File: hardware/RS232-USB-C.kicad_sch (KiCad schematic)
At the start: 68 parts, among them J1 USB_C_Receptacle_USB2.0_16P, J10 NC, J11 UART, J12 NC, J13 NC, J2 DE9_Receptacle, J3 NC, J4 RXTX, J5 RTSCTS, J6 DTRDSR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

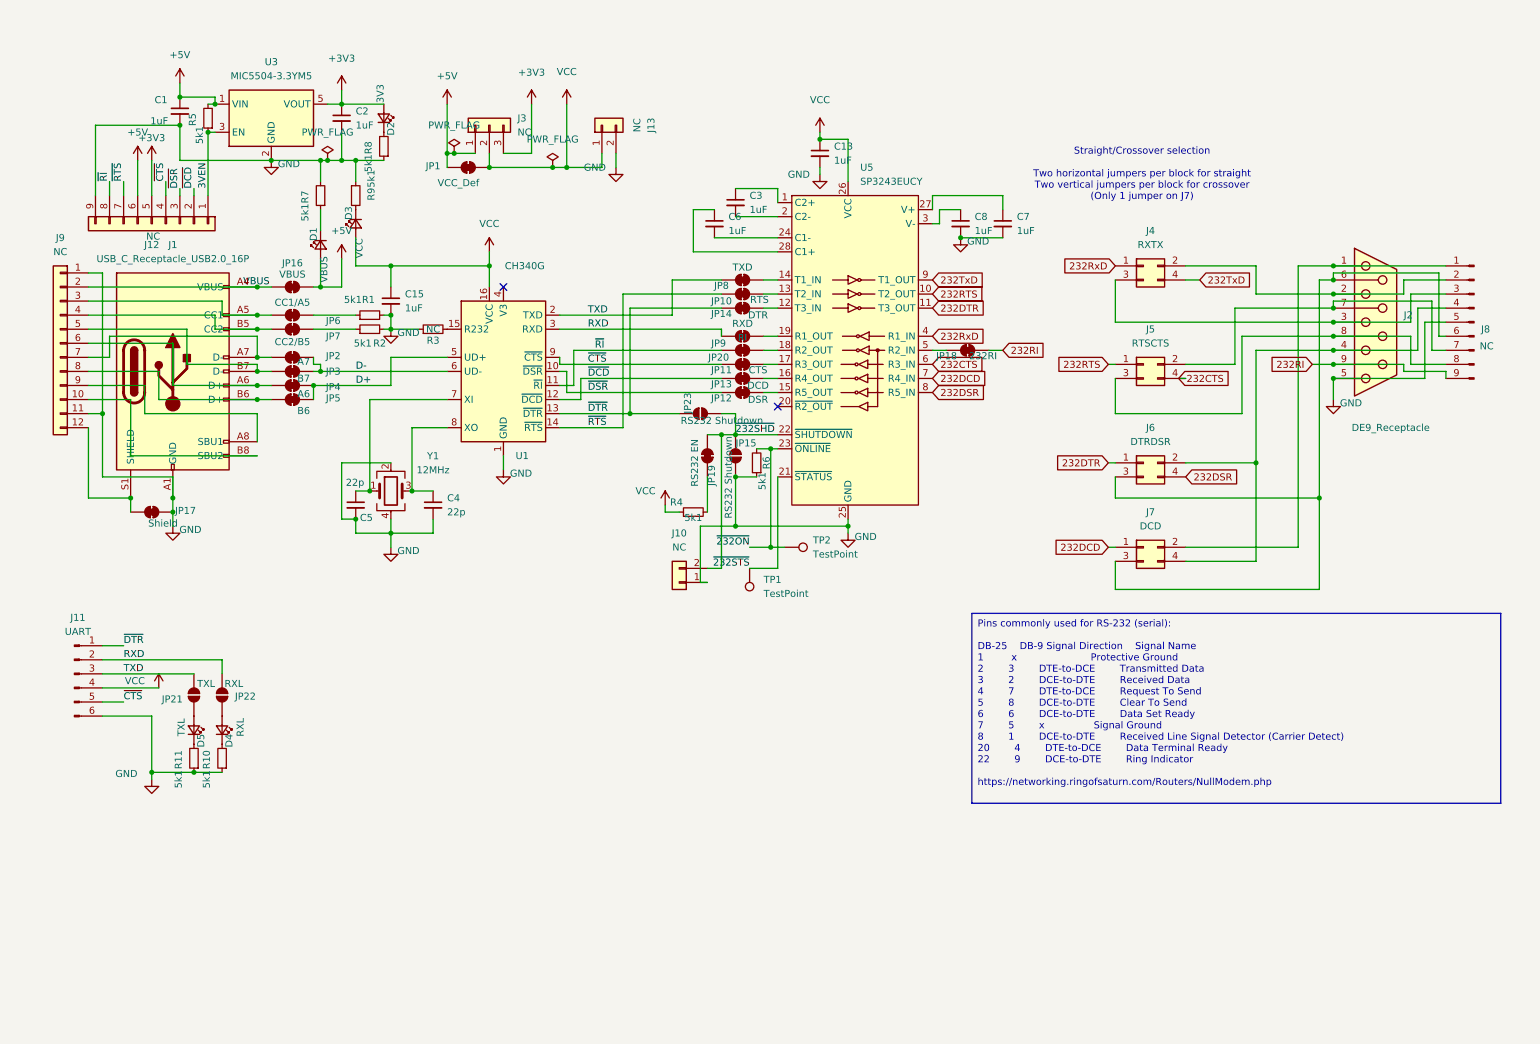
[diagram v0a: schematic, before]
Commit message: Tidy schematic
- Replaced criss-crossed wires with labels between IC/connectors
- Removed jumper 'values' where wasn't really needed
- repositioned references/values where hard to read
- gave components room to 'breathe'
- changed to regular (compared to small) components in most places to avoid cramping
- moved components around to be close to their logical section
- updated some symbols to be more standard/correct
- replaced 'NC' components to regularly labelled ones marked as DNP
- fixed sch->pcb linking on J3
- organized schematic into logical blocks
- uncommited the lockfile
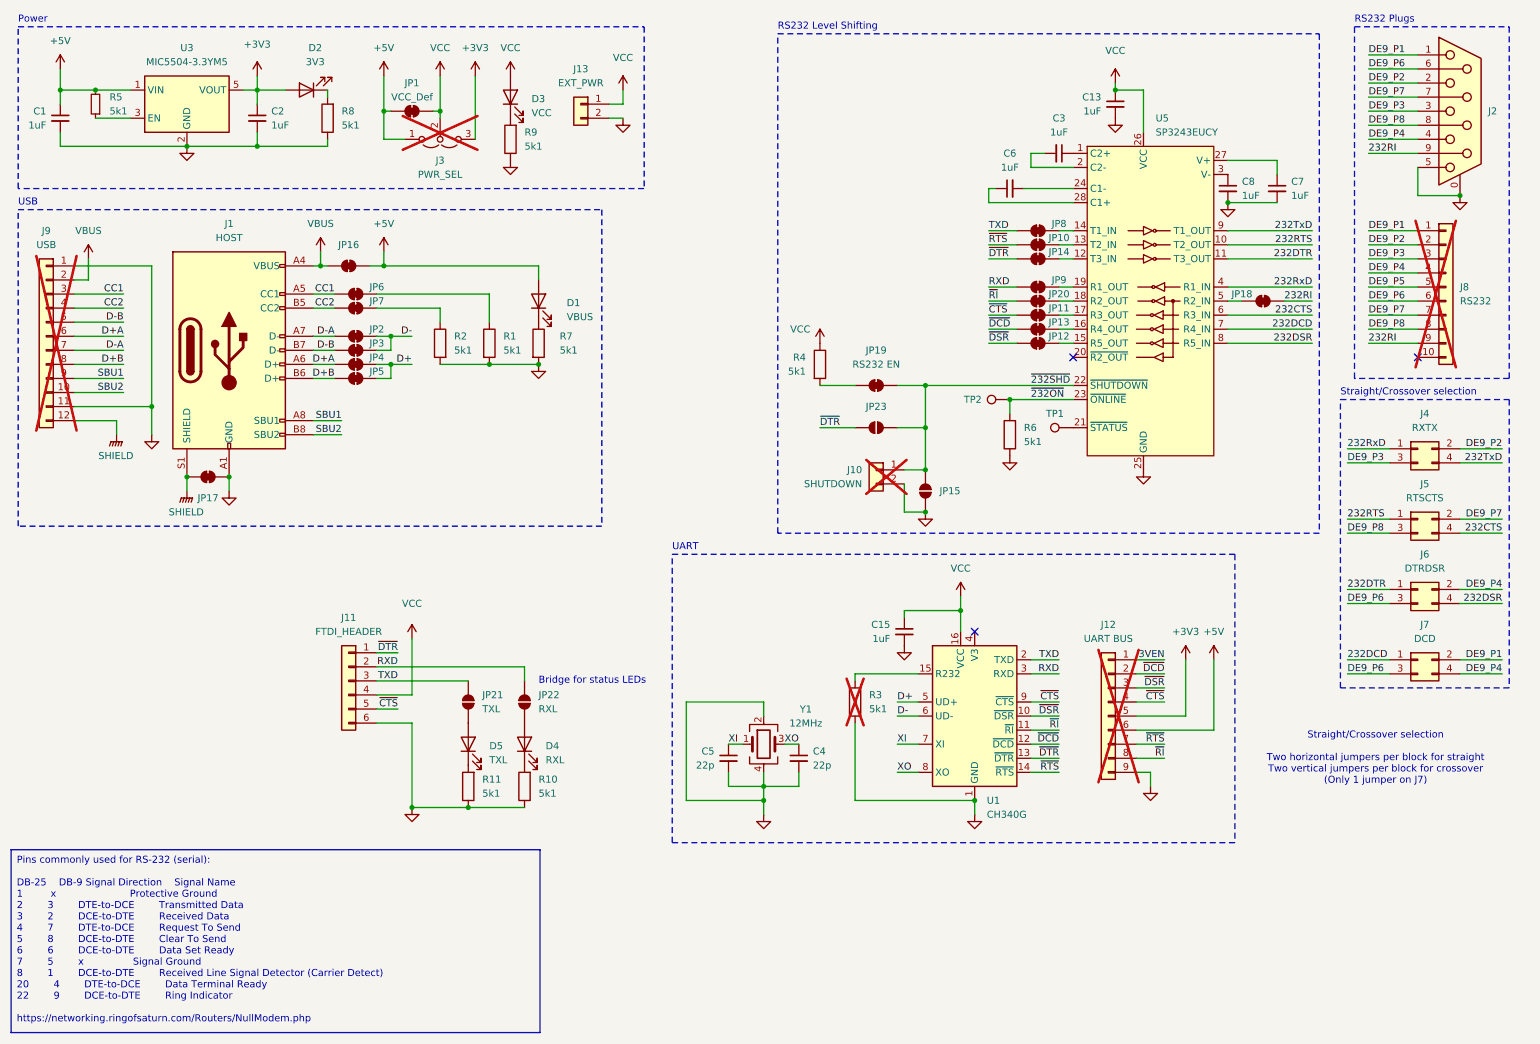
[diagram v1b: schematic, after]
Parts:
- D1, D2, D3, D4, D5: symbol Device:LED_Small -> Device:LED
- J1: value USB_C_Receptacle_USB2.0_16P -> HOST
- J10: value NC -> SHUTDOWN; now not fitted
- J11: value UART -> FTDI_HEADER; symbol Connector:Conn_01x06_Pin -> Connector_Generic:Conn_01x06
- J12: value NC -> UART BUS; now not fitted
- J13: value NC -> EXT_PWR
- J2: symbol Connector:DE9_Receptacle -> Connector:DE9_Receptacle_MountingHoles
- J3: value NC -> PWR_SEL; symbol Connector_Generic:Conn_01x03 -> Jumper:Jumper_3_Open; now not fitted; now left out of the parts list
- J8: value NC -> RS232; symbol Connector:Conn_01x09_Pin -> Connector_Generic:Conn_01x10; now not fitted
- J9: value NC -> USB; now not fitted
- R1, R10, R11, R2, R4, R6, R7, R8, R9: symbol Device:R_Small -> Device:R
- R3: value NC -> 5k1; symbol Device:R_Small -> Device:R; now not fitted
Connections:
- net 3VEN: no longer R5.1, U3.3 (EN)
- net GND: now also J10.2 (Pin_2), J2.0 (PAD); no longer J10.1 (Pin_1), J8.5 (Pin_5)
- net ~{232SHD}: now also J10.1 (Pin_1); no longer J10.2 (Pin_2)
- net DE9_P1: now reaches J2.1, J7.2 (Pin_2), J8.1 (Pin_1)
- net DE9_P2: now reaches J2.2, J4.2 (Pin_2), J8.2 (Pin_2)
- net DE9_P3: now reaches J2.3, J4.3 (Pin_3), J8.3 (Pin_3)
- net DE9_P4: now reaches J2.4, J6.2 (Pin_2), J7.4 (Pin_4), J8.4 (Pin_4)
- net DE9_P6: now reaches J2.6, J6.3 (Pin_3), J7.3 (Pin_3), J8.6 (Pin_6)
- net DE9_P7: now reaches J2.7, J5.2 (Pin_2), J8.7 (Pin_7)
- net DE9_P8: now reaches J2.8, J5.3 (Pin_3), J8.8 (Pin_8)
- net XI: now reaches C5.1, U1.7 (XI), Y1.1
- net XO: now reaches C4.1, U1.8 (XO), Y1.3
- net CC2: now reaches J1.B5 (CC2), J9.4 (Pin_4), JP7.2 (B)
- net D+A: now reaches J1.A6 (D+), J9.6 (Pin_6), JP4.1 (A)
- net SBU2: now reaches J1.B8 (SBU2), J9.10 (Pin_10)
- net SHIELD: now reaches J1.S1 (SHIELD), J9.12 (Pin_12), JP17.1 (A)
- net CC1: now reaches J1.A5 (CC1), J9.3 (Pin_3), JP6.1 (A)
- net D-B: now reaches J1.B7 (D-), J9.5 (Pin_5), JP3.1 (A)
- net D-A: now reaches J1.A7 (D-), J9.7 (Pin_7), JP2.1 (A)
- net D+B: now reaches J1.B6 (D+), J9.8 (Pin_8), JP5.1 (A)
- net SBU1: now reaches J1.A8 (SBU1), J9.9 (Pin_9)
- net ~{232STS}: no longer names the net of TP1.1, U5.21 (~{STATUS})
- new net: R5.1, U3.3 (EN)
- new net DE9_P5: J8.5 (Pin_5)
- no-connect marks 2 -> 3
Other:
- note added: "Bridge for status LEDs"
- note added: "Power"
- note added: "RS232 Level Shifting"
- note added: "RS232 Plugs"
- note added: "Straight/Crossover selection"
- note added: "UART"
- note added: "USB"
- moved on the sheet: C1, C13, C15, C2, C3, C4, C5, C6, C7, C8, D1, D2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

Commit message: Rev 1
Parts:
- added C9: 100nF, Capacitor_SMD:C_0805_2012Metric, symbol Device:C_Small
- added JP24: 3v3 opt., Jumper:SolderJumper-2_P1.3mm_Open_RoundedPad1.0x1.5mm, symbol Jumper:SolderJumper_2_Open
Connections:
- net DE9_P5 is gone; now on net GND: J8.5 (Pin_5)
- net +3V3: now also J9.12 (Pin_12)
- net 3VEN: now also R5.1, U3.3 (EN)
- net GND: now also C9.2
- net SHIELD: no longer J9.12 (Pin_12)
- net VCC: now also JP24.2 (B)
- net at U1.4 (V3): now also C9.1, JP24.1 (A)
- no-connect marks 3 -> 2
